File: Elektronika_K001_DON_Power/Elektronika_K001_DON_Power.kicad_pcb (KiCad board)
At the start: 2 copper layers, 87.5 x 46.2 mm, 12 parts, among them J1 Power In (+12VDC), J2 Conn_01x05, U1 PSU5, U2 R-78CK5.0-0.5

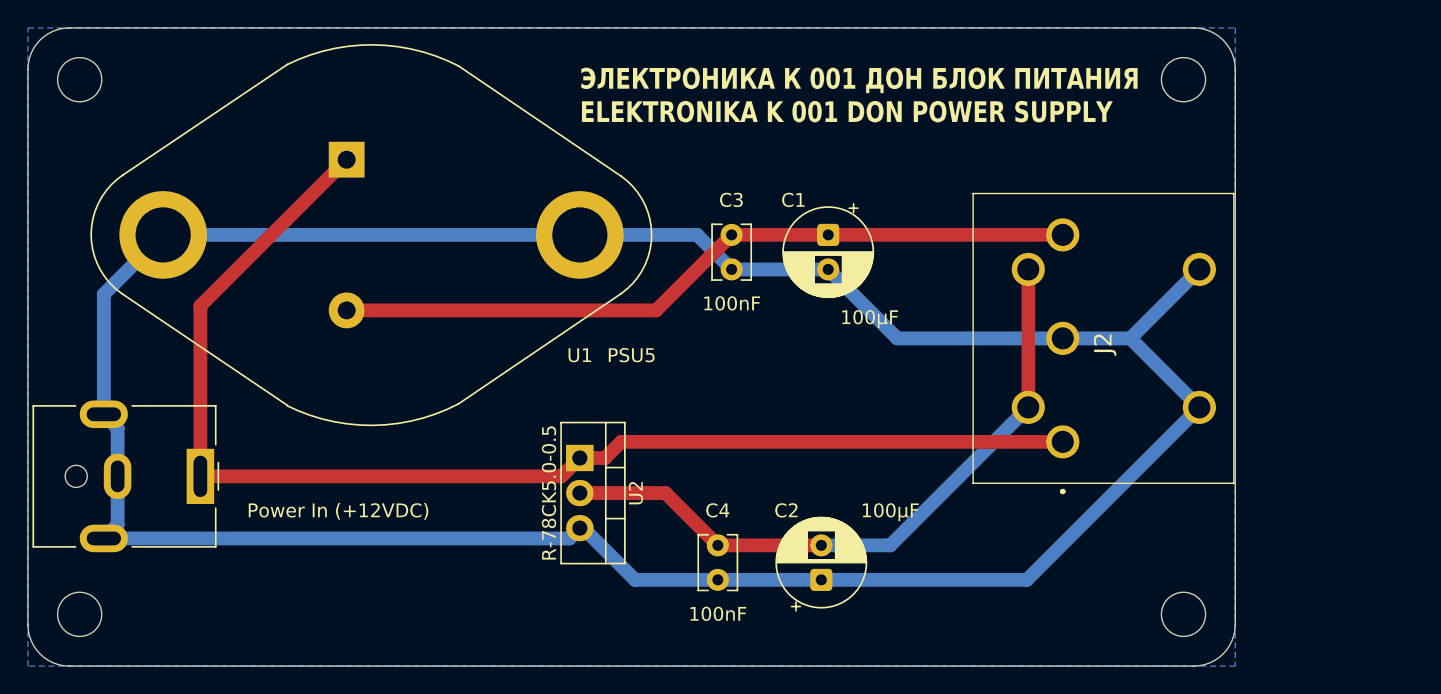
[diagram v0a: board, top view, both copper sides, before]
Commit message: Added fuse on 12V input
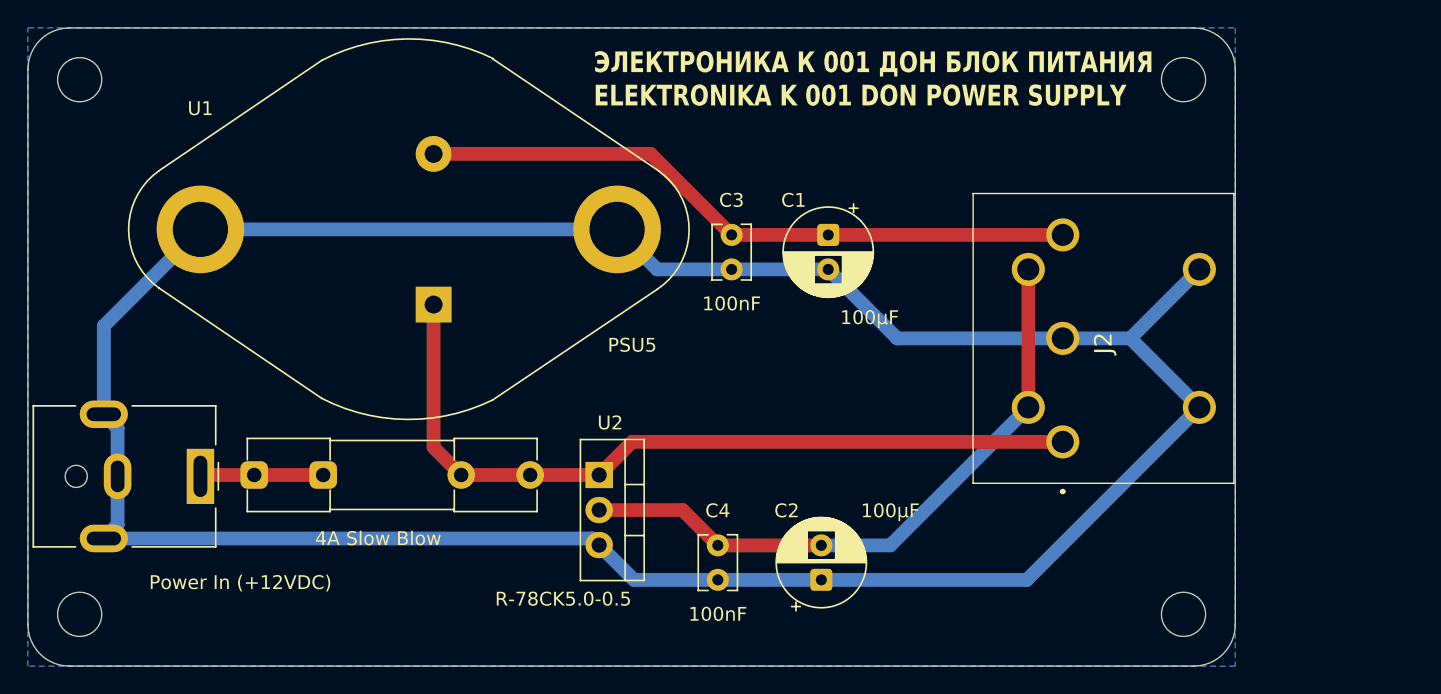
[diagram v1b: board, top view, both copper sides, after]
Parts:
- added F1: Fuse, Fuse:Fuseholder_Clip-5x20mm_Littelfuse_111_Inline_P20.00x5.00mm_D1.05mm_Horizontal, F.Cu at (121.4, 92.4)
- moved U1 12.2 mm to (134.4, 80.0), turned to 180 degrees
- moved U2 1.86 mm to (146.4, 92.4)
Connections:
- J1 pad 1: /+12V -> /+12V_{IN}
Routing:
- net /+12V: track 90.9 -> 57.8 mm
- net /+12V_{IN}: track 0.00 -> 8.94 mm
- net /+5V: track 54.2 -> 48.0 mm
- net /-5V: track 48.2 -> 46.3 mm
- net /GND: track 198.4 -> 196.8 mm
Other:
- board text added: "4A Slow Blow"
